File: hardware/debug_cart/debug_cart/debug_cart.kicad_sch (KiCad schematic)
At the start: 39 parts, among them CON1 vectrex-edge-connector, J1 USB_C_Receptacle_USB2.0, Q1 BSS138, Q2 BSS138, Q3 BSS138, U1 RP2040, U2 SN74LVC245APW, U3 SN74LVC245APW, U4 SN74LVC245APW, U5 AMS1117-3.3, U6 APS6404L-3SQRx-SN, U7 W25Q16JVSS, Y1 Crystal_GND24

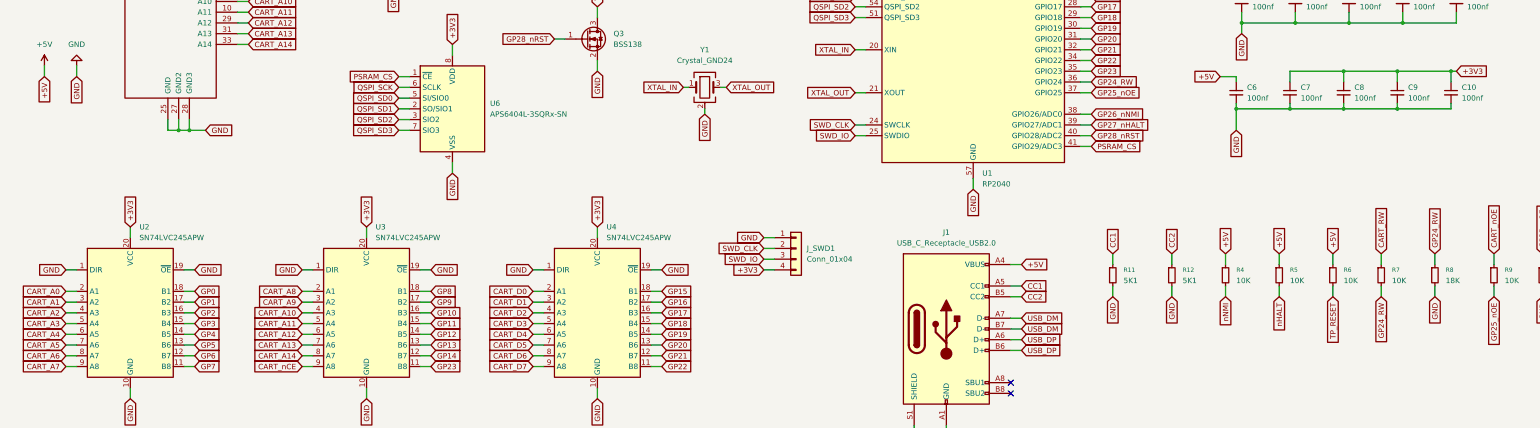
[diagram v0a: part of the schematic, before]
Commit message: hw(debug_cart): rewire U2/U3 DIR to ABUS_DIR for bus mastering
Single GPIO controls U2/U3 buffer direction (LOW=Vectrex→MCU ROM mode,
HIGH=MCU→Vectrex bus master mode). /OE of U2/U3 stays at GND.

- Remove R7/R8 (CART_RW divider): R/W sensing dropped (cart is read-only)
- New net ABUS_DIR connects U2.1, U3.1 and MCU pin GP24
- CART_RW now only present at CON1 card edge (NC on MCU side)

PCB netlist synced (3× ABUS_DIR labels in .pcb); physical routing pending.

Note: this checkpoint is taken BEFORE migrating U1 from RP2040 (QFN-56)
to RP2350A (QFN-60) — current .sch/.pcb still target RP2040 even though
firmware uses rp235x-hal.

Co-Authored-By: Claude Opus 4.7 <noreply@anthropic.com>
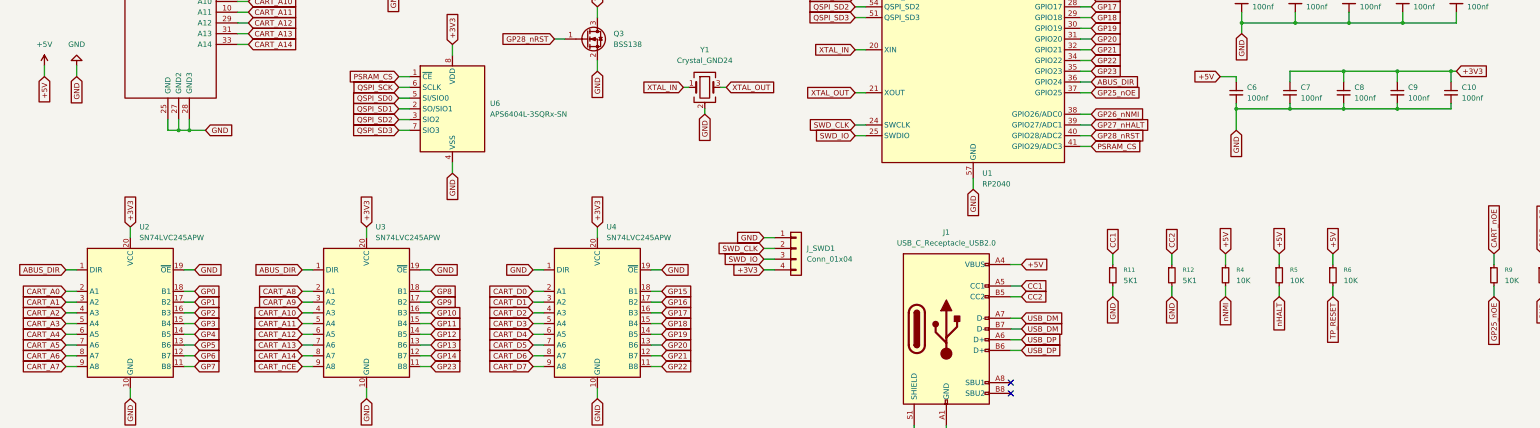
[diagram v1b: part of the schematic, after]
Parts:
- removed R7: 10K, Resistor_SMD:R_0805_2012Metric, symbol Device:R_Small
- removed R8: 18K, Resistor_SMD:R_0805_2012Metric, symbol Device:R_Small
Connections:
- net GND: no longer U2.1 (DIR), U3.1 (DIR)
- net GP24_RW renamed ABUS_DIR
- net ABUS_DIR: now also U2.1 (DIR), U3.1 (DIR)

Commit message: hw(debug_cart): semantic net labels + GPIO remap for cart-edge-facing MCU
LABELS: rename schematic global_labels from GPIO-based (GP0, GP24_ABUS_DIR)
to signal-meaningful names. Separates voltage domains clearly:

  5V Vectrex side (cart edge → buffer/transistor input): CART_* prefix
  3.3V MCU side (buffer output → MCU): semantic name (A0..A14, D0..D7,
    nCE, ABUS_DIR, DIR_CTRL, CART_RW_DRIVE, nOE_SENSE, *_DRIVE/*_SENSE)

Renamings applied (43 total):
- GP0..GP14   → A0..A14    (address bus, 3.3V side)
- GP15..GP22  → D0..D7     (data bus, 3.3V side)
- GP23        → nCE        (chip enable, 3.3V side)
- GP24_ABUS_DIR    → ABUS_DIR
- GP25_nOE         → nOE_SENSE
- GP26_nNMI        → nNMI_DRIVE
- GP27_nHALT       → nHALT_DRIVE
- GP28_nRST        → nRST_DRIVE
- GP29_DIR_CTRL    → DIR_CTRL
- GP30_CART_RW     → CART_RW_DRIVE
- GP31_PSRAM_CS    → PSRAM_CS
- GP32_UART0_TX    → UART_TX
- GP33_UART0_RX    → UART_RX
- GP34_SD_SCK      → SD_SCK
- GP35_SD_MOSI     → SD_MOSI
- GP36_SD_MISO     → SD_MISO
- GP37_SD_CS       → SD_CS
- GP38_SD_CD       → SD_CD
- GP39_PB6         → PB6_SENSE
- GP40_CART        → CART_SENSE
- GP41_nIRQ        → nIRQ_DRIVE

GPIO REMAP for QFN-80 rotation (side A faces card edge):
- A0..A14 → GP4..GP18 (was GP0..GP14) - side A of QFN-80
- nCE → GP19, ABUS_DIR → GP20 - last 2 GPIOs of side A
- D0..D7 → GP21..GP28 (was GP15..GP22) - side B
- DIR_CTRL → GP29, CART_RW_DRIVE → GP30, nOE_SENSE → GP31 - side B
- nHALT_DRIVE → GP0, nNMI_DRIVE → GP1, nRST_DRIVE → GP2, nIRQ_DRIVE → GP3 - side D
  (these drive BSS138 gates anywhere on board, no proximity needed)
- UART_TX/RX → GP39/GP40 (was GP32/GP33)
- PB6_SENSE → GP41, CART_SENSE → GP42 (was GP39/GP40)
- SD signals stay on side C (GP34-38)

Result: bus signals concentrate on sides A+B near the card edge, making
2-layer routing straightforward. Memories stay on side D (QSPI pinout
already there). Extras on side C. No physical conflicts.

Helper functions addr_to_gpio/gpio_to_addr/data_to_gpio/gpio_to_data
upd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
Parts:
- removed C_VREG1: 1 µF, Capacitor_SMD:C_0805_2012Metric, symbol Device:C_Small
- removed U1: RP2040, Package_DFN_QFN:QFN-56-1EP_7x7mm_P0.4mm_EP3.2x3.2mm, symbol MCU_RaspberryPi:RP2040
- added C11, C13, C15, C16, C17, C18, C19, C20: 100nf, Capacitor_SMD:C_0805_2012Metric, symbol Device:C_Small
- added C12: 1uf, Capacitor_SMD:C_0805_2012Metric, symbol Device:C_Small
- added C14: 10uf, Capacitor_SMD:C_0805_2012Metric, symbol Device:C_Small
- added C21, C22: 10nf, Capacitor_SMD:C_0805_2012Metric, symbol Device:C_Small
- added J2: Micro_SD_Card_Det_Hirose_DM3AT, Connector_Card:microSD_HC_Hirose_DM3AT-SF-PEJM5, symbol Connector:Micro_SD_Card_Det_Hirose_DM3AT
- added J_UART1: Conn_01x04, Connector_PinHeader_2.54mm:PinHeader_1x04_P2.54mm_Vertical, symbol Connector_Generic:Conn_01x04
- added Q4: BSS138, Package_TO_SOT_SMD:SOT-23, symbol Transistor_FET:BSS138
- added R10, R6: 10k, Resistor_SMD:R_0805_2012Metric, symbol Device:R_Small
- added R11, R13, R15: 10K, Resistor_SMD:R_0805_2012Metric, symbol Device:R_Small
- added R12, R14: 18K, Resistor_SMD:R_0805_2012Metric, symbol Device:R_Small
- added R9: 100K, Resistor_SMD:R_0805_2012Metric, symbol Device:R_Small
- added SW1: SW_Push, Button_Switch_SMD:SW_SPST_PTS810, symbol Switch:SW_Push
- added U1: RP2350B, Package_DFN_QFN:QFN-80-1EP_10x10mm_P0.4mm_EP3.4x3.4mm, symbol MCU_RaspberryPi:RP2350B
- added U8: 74LVC1G07, Package_TO_SOT_SMD:SOT-353_SC-70-5, symbol 74xGxx:74LVC1G07
- renumbered R4 to R1, R5 to R2, R6 to R3, R9 to R4, R10 to R5, R11 to R7, R12 to R8
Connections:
- net CART_7D is gone; now on net CART_D7: CON1.18 (D7)
- net CART_CE is gone; now on net CART_nCE: CON1.16 (CE)
- net CART_OE is gone; now on net CART_nOE: CON1.12 (OE)
- net nHALT is gone; now on net CART_nHALT: Q2.3 (D), R2.2
- net nNMI is gone; now on net CART_nNMI: Q1.3 (D), R1.2
- net +3V3: now also C5.1, C6.1, C11.1, C12.1, C13.1, C14.1, C15.1, C16.1, C17.1, C18.1, C19.1, C22.1, J2.4 (VDD), J_UART1.4 (Pin_4), R10.2, R9.1, U1.10 (DVDD), U1.15 (IOVDD), U1.24 (IOVDD), U1.29 (IOVDD), U1.32 (DVDD), U1.41 (IOVDD), U1.5 (IOVDD), U1.50 (IOVDD), U1.51 (DVDD), U1.60 (IOVDD), U1.61 (VREG_AVDD), U1.63 (VREG_LX), U1.65 (VREG_FB), U1.68 (USB_OTP_VDD), U1.69 (QSPI_IOVDD), U1.76 (IOVDD), U8.5 (VCC); no longer CON1.2 (VCC), CON1.4 (VCC2)
- net +5V: now also CON1.2 (VCC), CON1.4 (VCC2), C20.1, C21.1, R15.1, R6.2; no longer C5.1, C6.1
- net ABUS_DIR: now also U1.25 (GPIO24)
- net CART_CART: now also R13.1
- net CART_PB6: now also R11.1
- net CART_RW: now also R6.1, U8.4
- net DIR_CTRL: now also U4.1 (DIR), U1.37 (GPIO29)
- net GND: now also C11.2, C12.2, C13.2, C14.2, C15.2, C16.2, C17.2, C18.2, C19.2, C20.2, C21.2, C22.2, J2.6 (VSS), J2.9 (DET_B), J2.SH (SHIELD), J_UART1.1 (Pin_1), Q4.2 (S), R12.2, R14.2, SW1.2, U1.81 (GND), U8.3 (GND); no longer U4.1 (DIR)
- net PSRAM_CS: now also U1.39 (GPIO31)
- net QSPI_CSn: now also SW1.1, U1.75 (~{QSPI_SS})
- net QSPI_SCK: now also U1.71 (QSPI_SCLK)
- net QSPI_SD0: now also U1.72 (QSPI_SD0)
- net QSPI_SD1: now also U1.74 (QSPI_SD1)
- net QSPI_SD2: now also U1.73 (QSPI_SD2)
- net QSPI_SD3: now also U1.70 (QSPI_SD3)
- net SWD_CLK: now also U1.33 (SWCLK)
- net SWD_IO: now also U1.34 (SWDIO)
- net USB_DM: now also U1.66 (USB_DM)
- net USB_DP: now also U1.67 (USB_DP)
- net XTAL_IN: now also U1.30 (XIN)
- net XTAL_OUT: now also U1.31 (XOUT)
- net CART_HALT renamed CART_nHALT
- net CART_IRQ renamed CART_nIRQ
- net CART_nIRQ: now also Q4.3 (D), R15.2
- net CART_NMI renamed CART_nNMI
- net GP0 renamed A0
- net A0: now also U1.77 (GPIO0)
- net GP1 renamed A1
- net A1: now also U1.78 (GPIO1)
- net GP10 renamed A10
- net A10: now also U1.8 (GPIO10)
- net GP11 renamed A11
- net A11: now also U1.9 (GPIO11)
- net GP12 renamed A12
- net A12: now also U1.11 (GPIO12)
- net GP13 renamed A13
- net A13: now also U1.12 (GPIO13)
- net GP14 renamed A14
- net A14: now also U1.13 (GPIO14)
- net GP15 renamed D0
- net D0: now also U1.14 (GPIO15)
- net GP16 renamed D1
- net D1: now also U1.16 (GPIO16)
- net GP17 renamed D2
- net D2: now also U1.17 (GPIO17)
- net GP18 renamed D3
- net D3: now also U1.18 (GPIO18)
- net GP19 renamed D4
- net D4: now also U1.19 (GPIO19)
- net GP2 renamed A2
- net A2: now also U1.79 (GPIO2)
- net GP20 renamed D5
- net D5: now also U1.20 (GPIO20)
- net GP21 renamed D6
- net D6: now also U1.21 (GPIO21)
- net GP22 renamed D7
- net D7: now also U1.22 (GPIO22)
- net GP23 renamed nCE
- net nCE: now also U1.23 (GPIO23)
- net GP25_nOE renamed nOE_SENSE
- net nOE_SENSE: now also U1.26 (GPIO25)
- net GP26_nNMI renamed nNMI_DRIVE
- net nNMI_DRIVE: now also U1.27 (GPIO26)
- net GP27_nHALT renamed nHALT_DRIVE
- net nHALT_DRIVE: now also U1.28 (GPIO27)
- net GP28_nRST renamed nRST_DRIVE
- net nRST_DRIVE: now also U1.36 (GPIO28)
- net GP3 renamed A3
- net A3: now also U1.80 (GPIO3)
- net GP4 renamed A4
- net A4: now also U1.1 (GPIO4)
- net GP5 renamed A5
- net A5: now also U1.2 (GPIO5)
- net GP6 renamed A6
- net A6: now also U1.3 (GPIO6)
- net GP7 renamed A7
- net A7: now also U1.4 (GPIO7)
- net GP8 renamed A8
- net A8: now also U1.6 (GPIO8)
- net GP9 renamed A9
- net A9: now also U1.7 (GPIO9)
- new net CART_RW_DRIVE: U1.38 (GPIO30), U8.2
- new net CART_SENSE: R13.2, R14.1, U1.49 (GPIO40/ADC0)
- new net PB6_SENSE: R11.2, R12.1, U1.48 (GPIO39)
- new net RUN: R9.2, U1.35 (RUN)
- new net SD_CD: J2.10 (DET_A), U1.47 (GPIO38)
- new net SD_CS: J2.2 (DAT3/CD), R10.1, U1.46 (GPIO37)
- new net SD_MISO: J2.7 (DAT0), U1.45 (GPIO36)
- new net SD_MOSI: J2.3 (CMD), U1.44 (GPIO35)
- new net SD_SCK: J2.5 (CLK), U1.43 (GPIO34)
- new net UART_RX: J_UART1.2 (Pin_2), U1.42 (GPIO33)
- new net UART_TX: J_UART1.3 (Pin_3), U1.40 (GPIO32)
- new net nIRQ_DRIVE: Q4.1 (G), U1.52 (GPIO41/ADC1)
- no-connect marks 2 -> 14
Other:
- note added: "CON1 CART CONN"
- note added: "FLASH"
- note added: "J1 USB-C"
- note added: "J2 SD Card"
- note added: "J_SWD1"
- note added: "J_UART1"
- note added: "MCU"
- note added: "POWER"
- note added: "PSRAM"
- note added: "Q1 (BSS138 CART_nNMI)"
- note added: "Q2 (BSS138 CART_nHALT)"
- note added: "Q3 (BSS138 nRST)"
- note added: "Q4 (BSS138 IRQ)"
- note added: "SW1 Push Switch"
- note added: "Somewhere in 2026"
- note added: "U1 ADC_AVDD"
- note added: "U1 DVDD"
- note added: "U1 IOVDD"
- note added: "U1 QSPI_IOVDD"
- note added: "U1 USB_OTP_VDD"
- note added: "U1 VREG_AVDD"
- note added: "U1 VREG_VIN"
- note added: "U2 (74LVC245A)"
- note added: "U3 (74LVC245A)"
- note added: "U4 (74LVC245A)"
- note added: "U5 (AMS1117-3.3)"
- note added: "U8 (74LVC1G07)"
- note added: "Vectrex RP2350 debug cart"
- note added: "Y1 Oscillator"
- moved on the sheet: C1, C2, C3, C4, H1, H2, H3, H4, H5, J1, J_SWD1, Q1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

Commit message: hw(debug_cart): full PCB layout — 4 layers, all components placed and routed
PCB stackup upgraded to 4 layers for cleaner routing of the Vectrex bus,
QSPI memory bus, and USB differential pair:
  - F.Cu (top signal + components)
  - In1.Cu (GND plane)
  - In2.Cu (+3V3 plane)
  - B.Cu (bottom signal + decoupling)

Final BOM (all references):
  ICs:       U1 RP2350B, U2/U3/U4 74LVC245A buffers, U5 AMS1117 LDO,
             U6 APS6404L PSRAM, U7 W25Q64JV flash, U8 74LVC1G07 1-gate
  Transistors: Q1-Q4 BSS138 (HALT/NMI/RST/IRQ open-drain)
  Resistors: R1-R15 (4× BSS138 pullups, /OE divider, CART_RW pullup,
             USB-C CC pulldowns, RUN pullup, SD_CS pullup, PB6/CART
             dividers, IRQ pullup)
  Caps:      C1-C24 (MCU decoupling per rail, U6/U7 decoupling,
             3× decoupling for new RP2350B rails, SD bulk, LDO bulks,
             crystal load caps)
  Connectors: CON1 card edge (DNP for BOM), J1 USB-C, J2 microSD,
             J_UART1 1×4 header, J_SWD1 SWD header
  Other:     SW1 BOOTSEL button, Y1 12MHz crystal + load caps,
             TP_BOOTSEL + TP_RESET test points

Schematic ERC: 0 errors, 0 warnings (2 LDO bypass mode exclusions noted)
PCB DRC:       0 errors, 0 warnings

All components match COMPONENTS.md / pins.rs / MIGRATION_*.md docs.

The cart edge uses ENIG gold finger plating with 45° bevel (specified at
fabrication time, not in the design). PCB ready for Gerber generation.

Co-Authored-By: Claude Opus 4.7 <noreply@anthropic.com>
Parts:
- removed H1, H2, H3, H4: MountingHole, vextreme:Mounting_Hole_D3.7mm, symbol Mechanical:MountingHole
- removed H5: MountingHole, vextreme:Mounting_Hole_D5.2mm, symbol Mechanical:MountingHole
- added C23, C24: 22pf, Capacitor_SMD:C_0402_1005Metric, symbol Device:C_Small
- C1, C10, C11, C12, C13, C14, C15, C16, C17, C18, C19, C2, C20, C21, C22, C3, C4, C5, C6, C7, C8, C9: footprint Capacitor_SMD:C_0805_2012Metric -> Capacitor_SMD:C_0603_1608Metric
- R1, R10, R11, R12, R13, R14, R15, R2, R3, R4, R5, R6, R7, R8, R9: footprint Resistor_SMD:R_0805_2012Metric -> Resistor_SMD:R_0603_1608Metric
- U6: value APS6404L-3SQRx-SN -> APS6404L-3SQR-SN
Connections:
- net +3V3: now also U1.59 (ADC_AVDD), U1.64 (VREG_VIN)
- net A0: now also U1.1 (GPIO4); no longer U1.77 (GPIO0)
- net A1: now also U1.2 (GPIO5); no longer U1.78 (GPIO1)
- net A10: now also U1.13 (GPIO14); no longer U1.8 (GPIO10)
- net A11: now also U1.14 (GPIO15); no longer U1.9 (GPIO11)
- net A12: now also U1.16 (GPIO16); no longer U1.11 (GPIO12)
- net A13: now also U1.17 (GPIO17); no longer U1.12 (GPIO13)
- net A14: now also U1.18 (GPIO18); no longer U1.13 (GPIO14)
- net A2: now also U1.3 (GPIO6); no longer U1.79 (GPIO2)
- net A3: now also U1.4 (GPIO7); no longer U1.80 (GPIO3)
- net A4: now also U1.6 (GPIO8); no longer U1.1 (GPIO4)
- net A5: now also U1.7 (GPIO9); no longer U1.2 (GPIO5)
- net A6: now also U1.8 (GPIO10); no longer U1.3 (GPIO6)
- net A7: now also U1.9 (GPIO11); no longer U1.4 (GPIO7)
- net A8: now also U1.11 (GPIO12); no longer U1.6 (GPIO8)
- net A9: now also U1.12 (GPIO13); no longer U1.7 (GPIO9)
- net ABUS_DIR: now also U1.20 (GPIO20); no longer U1.25 (GPIO24)
- net CART_SENSE: now also U1.53 (GPIO42/ADC2); no longer U1.49 (GPIO40/ADC0)
- net D0: now also U1.21 (GPIO21); no longer U1.14 (GPIO15)
- net D1: now also U1.22 (GPIO22); no longer U1.16 (GPIO16)
- net D2: now also U1.23 (GPIO23); no longer U1.17 (GPIO17)
- net D3: now also U1.25 (GPIO24); no longer U1.18 (GPIO18)
- net D4: now also U1.26 (GPIO25); no longer U1.19 (GPIO19)
- net D5: now also U1.27 (GPIO26); no longer U1.20 (GPIO20)
- net D6: now also U1.28 (GPIO27); no longer U1.21 (GPIO21)
- net D7: now also U1.36 (GPIO28); no longer U1.22 (GPIO22)
- net GND: now also C23.1, C24.1
- net PB6_SENSE: now also U1.52 (GPIO41/ADC1); no longer U1.48 (GPIO39)
- net PSRAM_CS: now also U1.77 (GPIO0); no longer U1.39 (GPIO31)
- net UART_RX: now also U1.49 (GPIO40/ADC0); no longer U1.42 (GPIO33)
- net UART_TX: now also U1.48 (GPIO39); no longer U1.40 (GPIO32)
- net XTAL_IN: now also C23.2
- net XTAL_OUT: now also C24.2
- net nCE: now also U1.19 (GPIO19); no longer U1.23 (GPIO23)
- net nHALT_DRIVE: now also U1.78 (GPIO1); no longer U1.28 (GPIO27)
- net nIRQ_DRIVE: now also U1.40 (GPIO32); no longer U1.52 (GPIO41/ADC1)
- net nNMI_DRIVE: now also U1.79 (GPIO2); no longer U1.27 (GPIO26)
- net nOE_SENSE: now also U1.39 (GPIO31); no longer U1.26 (GPIO25)
- net nRST_DRIVE: now also U1.80 (GPIO3); no longer U1.36 (GPIO28)
- no-connect marks 14 -> 12
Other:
- moved on the sheet: Y1
